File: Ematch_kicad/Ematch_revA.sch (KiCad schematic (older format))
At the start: 12 parts, among them U1 TPS22929D, U2 TPS22929D, U3 INA138

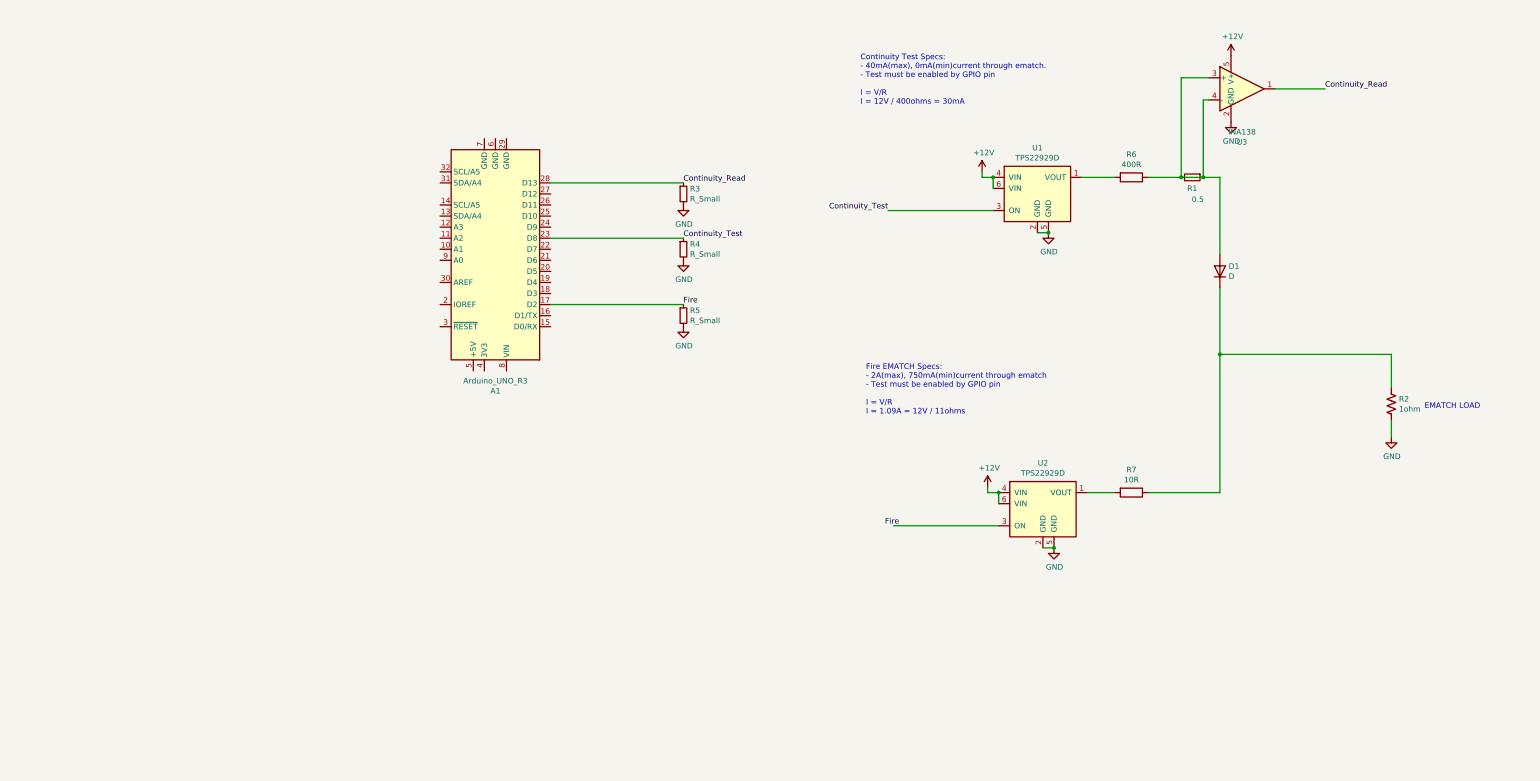
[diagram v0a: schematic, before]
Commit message: Added discrete switch
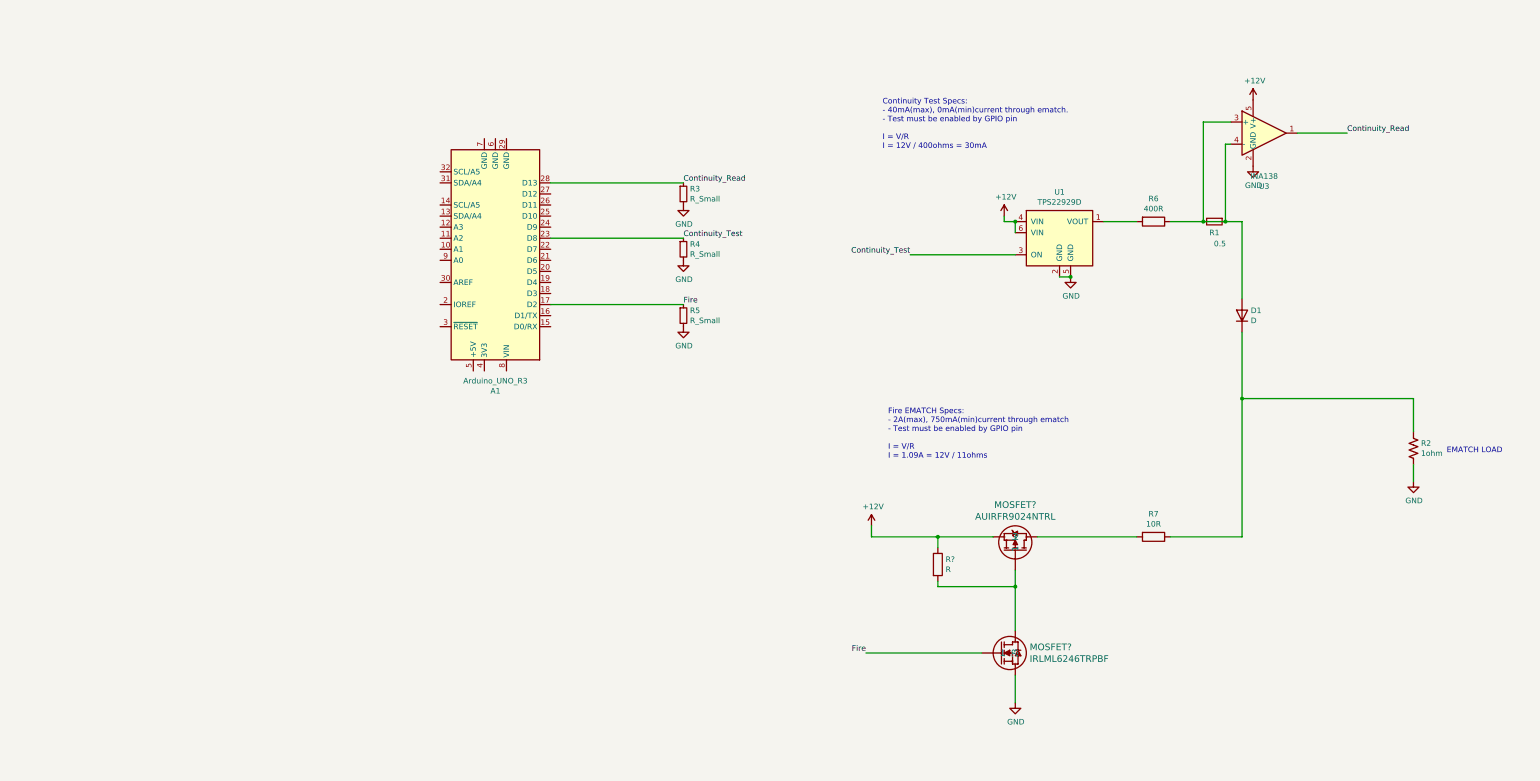
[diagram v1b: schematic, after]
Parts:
- removed U2: TPS22929D, Package_TO_SOT_SMD:SOT-23-6, symbol Power_Management:TPS22929D
- added MOSFET?: IRLML6246TRPBF, MICRO3_SOT-23_INF, symbol IRLML6246TRPBF_nmos:IRLML6246TRPBF
- added MOSFET?: AUIRFR9024NTRL, D-PAK_TO-252AA_INF, symbol AUIRFR9024NTR_pmos:AUIRFR9024NTRL
- added R?: R, symbol Device:R
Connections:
- wire segments 30 -> 35
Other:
- moved on the sheet: D1, R1, R2, R6, R7, U1, U3

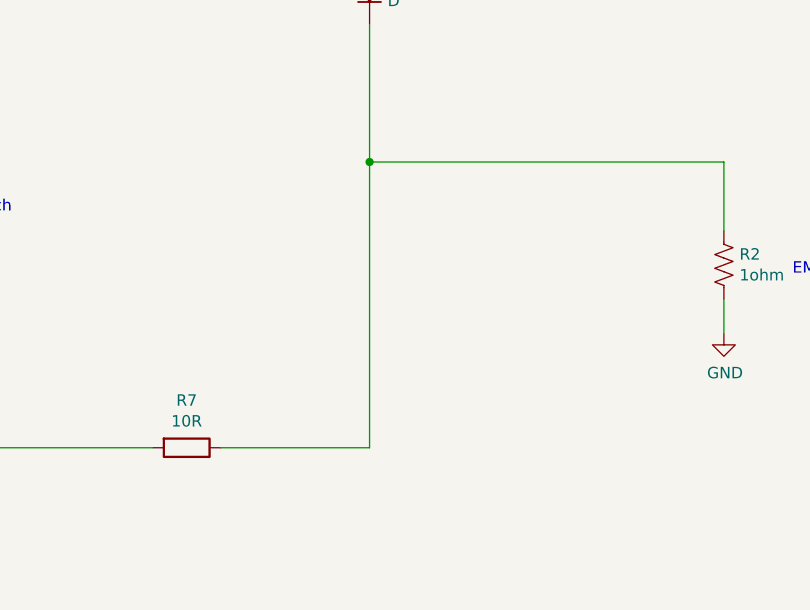
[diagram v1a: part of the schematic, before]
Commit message: Added discrete switch
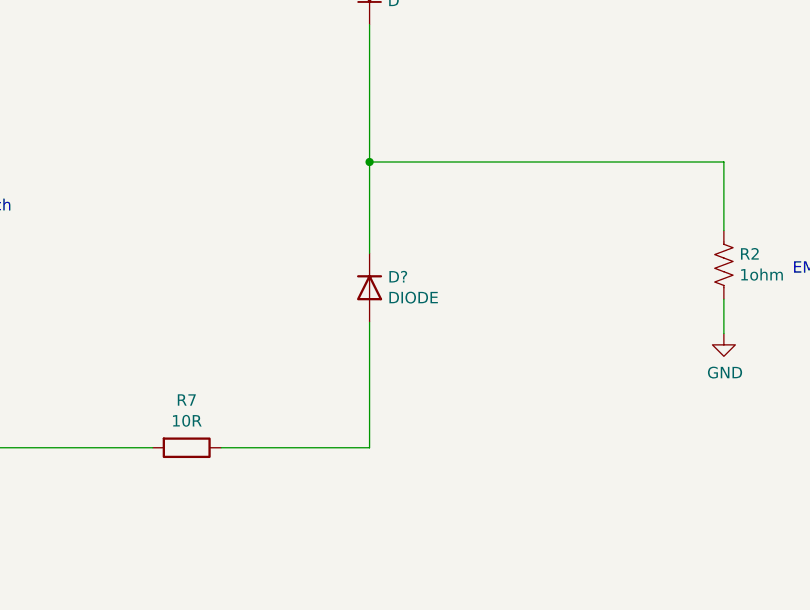
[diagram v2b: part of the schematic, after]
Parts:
- added D?: DIODE, symbol Simulation_SPICE:DIODE
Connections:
- net at D1.1 (K), R2.1: now also D?.2 (K); no longer R7.1
- new net: D?.1 (A), R7.1
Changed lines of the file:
@@
 Fire EMATCH Specs:\n- 2A(max), 750mA(min)current through ematch\n- Test must be enabled by GPIO pin\n\nI = V/R\nI = 1.09A = 12V / 11ohms
 Wire Wire Line
-	8250 3950 8250 5200
+	8250 3950 8250 4350
 Wire Wire Line
 	8250 2350 8250 3050
@@
 	1    0    0    -1
 $EndComp
+$Comp
+L Simulation_SPICE:DIODE D?
+U 1 1 60F672A5
+P 8250 4500
+F 0 "D?" V 8296 4420 50  0000 R CNN
+F 1 "DIODE" V 8205 4420 50  0000 R CNN
+F 2 "" H 8250 4500 50  0001 C CNN
+F 3 "~" H 8250 4500 50  0001 C CNN
+F 4 "Y" H 8250 4500 50  0001 L CNN "Spice_Netlist_Enabled"
+F 5 "V" H 8250 4500 50  0001 L CNN "Spice_Primitive"
+	1    8250 4500
+	0    -1   -1   0
+$EndComp
+Wire Wire Line
+	8250 4650 8250 5200
 $EndSCHEMATC

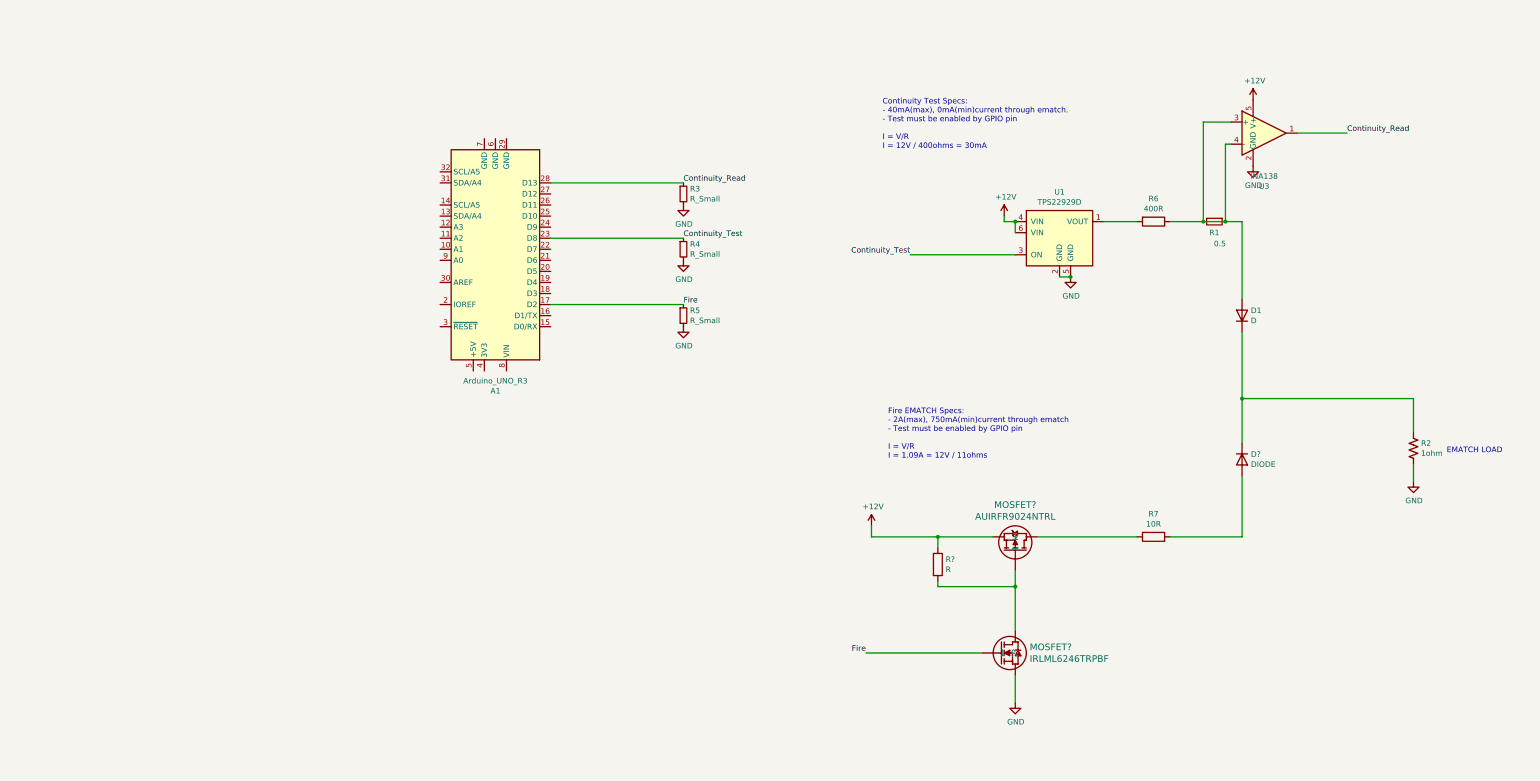
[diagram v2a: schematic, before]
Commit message: Added pcb layout and improved schematic
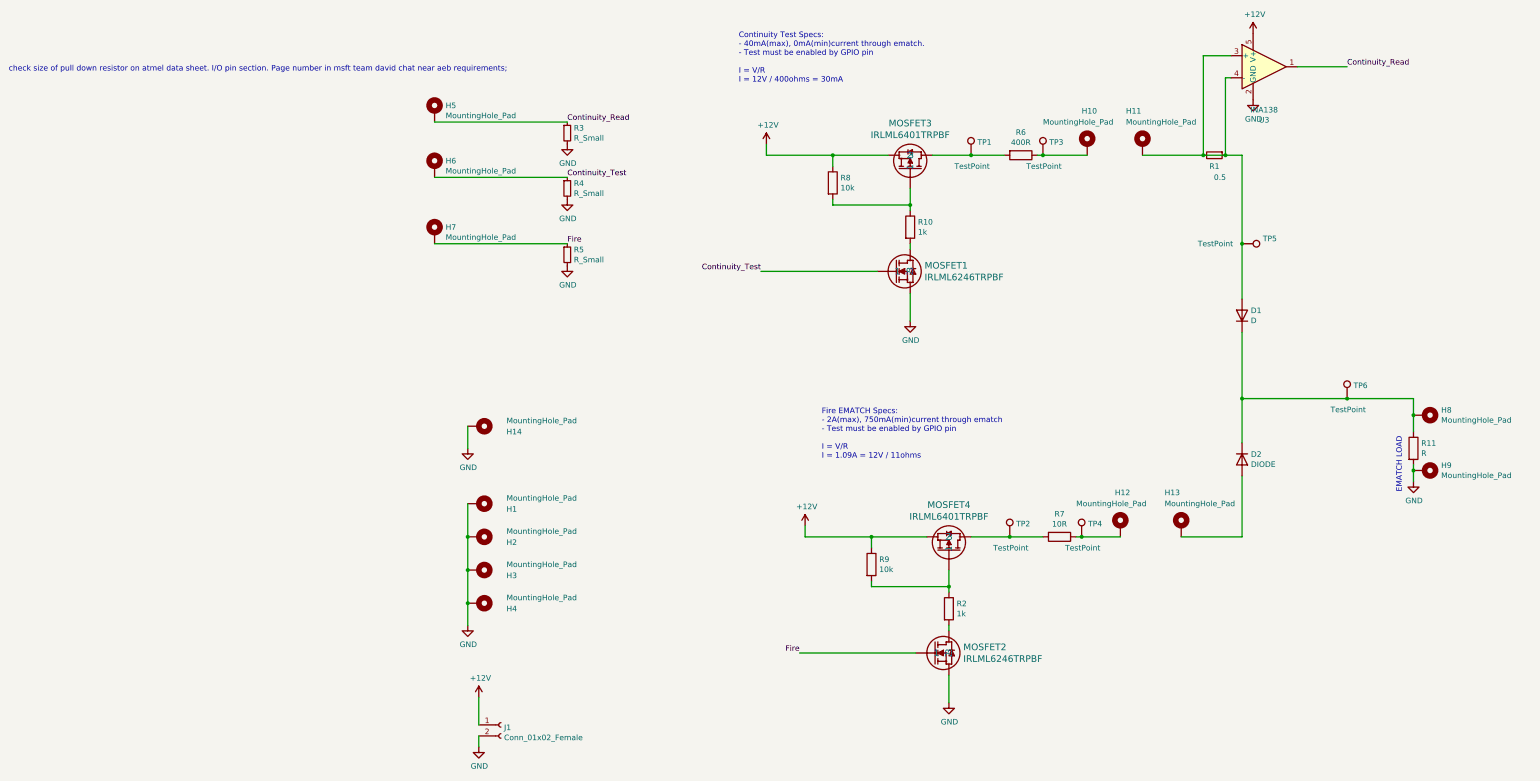
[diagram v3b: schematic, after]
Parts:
- removed A1: Arduino_UNO_R3, Module:Arduino_UNO_R3, symbol MCU_Module:Arduino_UNO_R3
- removed MOSFET?: AUIRFR9024NTRL, D-PAK_TO-252AA_INF, symbol AUIRFR9024NTR_pmos:AUIRFR9024NTRL
- removed R2: 1ohm, symbol Device:R_US
- removed U1: TPS22929D, Package_TO_SOT_SMD:SOT-23-6, symbol Power_Management:TPS22929D
- added H1, H2, H3, H4: MountingHole_Pad, MountingHole:MountingHole_2.5mm_Pad_Via, symbol Mechanical:MountingHole_Pad
- added H10, H11, H12, H13: MountingHole_Pad, Connector_Pin:Pin_D1.3mm_L11.0mm, symbol Mechanical:MountingHole_Pad
- added H14, H5, H6, H7, H8, H9: MountingHole_Pad, Connector_Pin:Pin_D1.0mm_L10.0mm, symbol Mechanical:MountingHole_Pad
- added J1: Conn_01x02_Female, Connector_USB:USB_C_Plug_Molex_105444, symbol Connector:Conn_01x02_Female
- added MOSFET1: IRLML6246TRPBF, Package_TO_SOT_SMD:TSOT-23, symbol IRLML6246TRPBF_nmos:IRLML6246TRPBF
- added MOSFET3, MOSFET4: IRLML6401TRPBF, Package_TO_SOT_SMD:TSOT-23, symbol pmos_ematch:IRLML6401TRPBF
- added R10, R2: 1k, Resistor_SMD:R_0805_2012Metric_Pad1.15x1.40mm_HandSolder, symbol Device:R
- added R11: R, Resistor_THT:R_Axial_DIN0411_L9.9mm_D3.6mm_P15.24mm_Horizontal, symbol Device:R
- added R8: 10k, Resistor_SMD:R_0805_2012Metric_Pad1.15x1.40mm_HandSolder, symbol Device:R
- added TP1, TP2, TP3, TP4, TP5, TP6: TestPoint, TestPoint:TestPoint_Pad_D1.5mm, symbol Connector:TestPoint
- D1: footprint (none) -> Diode_SMD:D_0805_2012Metric_Pad1.15x1.40mm_HandSolder
- D2: renamed from D?; footprint (none) -> Diode_SMD:D_0805_2012Metric_Pad1.15x1.40mm_HandSolder
- MOSFET2: renamed from MOSFET?; footprint MICRO3_SOT-23_INF -> Package_TO_SOT_SMD:TSOT-23
- R1, R3, R4, R5, R6, R7: footprint (none) -> Resistor_SMD:R_0805_2012Metric_Pad1.15x1.40mm_HandSolder
- R9: renamed from R?; value R -> 10k; footprint (none) -> Resistor_SMD:R_0805_2012Metric_Pad1.15x1.40mm_HandSolder
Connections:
- net +12V: now also J1.1 (Pin_1), MOSFET3.2, MOSFET4.2, R8.1
- net Continuity_Read: now also H5.1
- net Continuity_Test: now also H6.1, MOSFET1.1
- net Fire: now also H7.1
- net GND: now also H1.1, H14.1, H2.1, H3.1, H4.1, H9.1, J1.2 (Pin_2), MOSFET1.2, R11.2
- net at D1.1 (K), D2.2 (K): now also H8.1, R11.1, TP6.1
- net at D1.2 (A), R1.1, R1.2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: now also H11.1, TP5.1; no longer R6.1
- net at MOSFET2.3: now also R2.2; no longer R9.2
- net at R6.2: now also MOSFET3.3, TP1.1
- net at R7.2: now also MOSFET4.3, TP2.1
- net at D2.1 (A): now also H13.1; no longer R7.1
- new net: MOSFET4.1, R2.1, R9.2
- new net: MOSFET1.3, R10.2
- new net: MOSFET3.1, R10.1, R8.2
- new net: H10.1, R6.1, TP3.1
- new net: H12.1, R7.1, TP4.1
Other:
- note added: "check size of pull down resistor on atmel data sheet. I/O pin section. Page number in msft team david chat near aeb requirements;"
- moved on the sheet: MOSFET2, R1, R3, R4, R5, R6, R9, U3
